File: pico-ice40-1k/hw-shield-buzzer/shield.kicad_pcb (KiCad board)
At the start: 2 copper layers, 58.4 x 41.3 mm, 31 parts, among them J1 JACK_TRS_6PINS, P1 CONN_01X12, P2 CONN_01X12, SW1 SPST, SW2 SW_PUSH, U1 TLV320DAC3203, U2 LD39015M18R, U3 SSM2305, U4 SSM2305

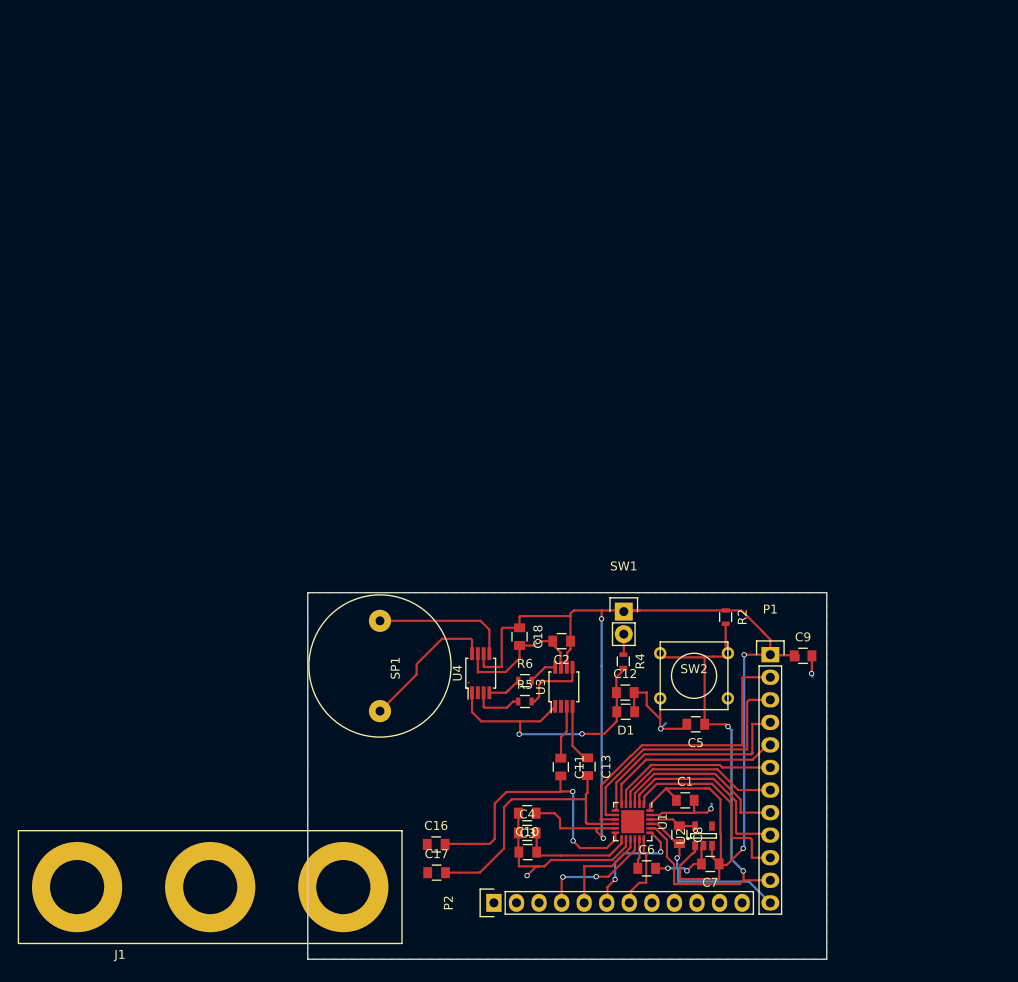
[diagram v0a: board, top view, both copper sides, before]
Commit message: new schema and PCB with lib for jack connector
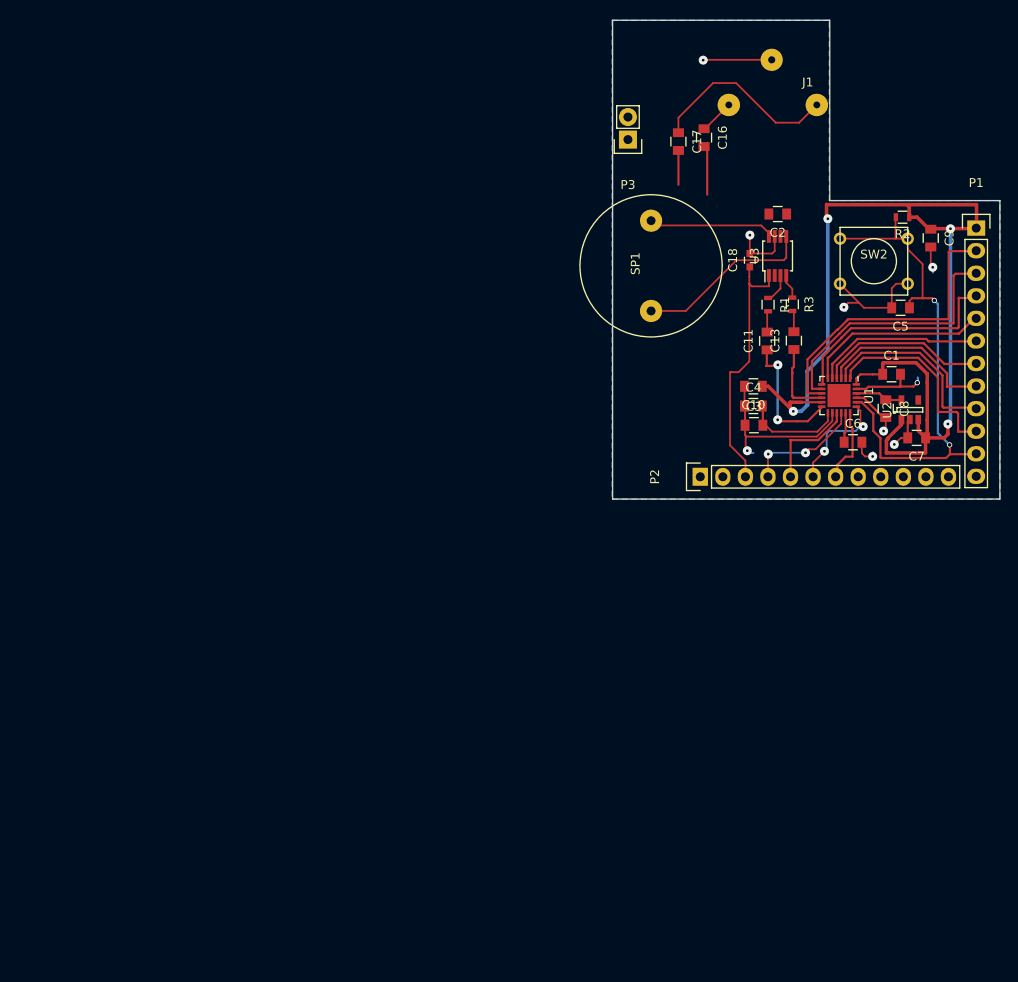
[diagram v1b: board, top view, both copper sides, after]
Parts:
- removed C12: 1u, Capacitors_SMD:C_0805
- removed D1: LED, Capacitors_SMD:C_0805
- removed R4: 1k, Resistors_SMD:R_0603
- removed R5, R6: 25k, Resistors_SMD:R_0603
- removed SW1: SPST, Pin_Headers:Pin_Header_Straight_1x02
- removed U4: SSM2305, Housings_SSOP:MSOP-8_3x3mm_Pitch0.65mm
- added P3: CONN_01X02, Pin_Headers:Pin_Header_Straight_1x02, F.Cu at (157.3, 63.9)
- added R1: 110k, Resistors_SMD:R_0603, F.Cu at (173.1, 82.5)
- added R3: 110k, Resistors_SMD:R_0603, F.Cu at (175.8, 82.5)
- C18: value 0.1u -> 1u; footprint Capacitors_SMD:C_0805 -> Capacitors_SMD:C_0603
- J1: footprint Connect:Banana_Jack_3Pin -> shield_foorprint:Jack Cliff FC68131
- U3: value SSM2305 -> TPA2005D1
- moved J1 113.0 mm to (167.4, 50.6), turned to 0 degrees
- moved C17 86.7 mm to (163.0, 64.2), turned to 270 degrees
- moved C16 85.1 mm to (165.9, 63.7), turned to 270 degrees
- moved SP1 54.4 mm to (159.9, 78.1), turned to 90 degrees
- moved C3 54.4 mm to (171.5, 96.1)
- moved C10 54.4 mm to (171.4, 91.7)
- moved C4 54.4 mm to (171.4, 93.9)
- moved U3 54.1 mm to (174.2, 77.0)
- moved C2 53.9 mm to (174.2, 72.3)
- moved P1 53.3 mm to (196.5, 73.9)
- moved U1 53.3 mm to (181.1, 92.7)
- moved C13 53.3 mm to (176.0, 86.6), turned to 90 degrees
- moved C6 53.3 mm to (182.7, 98.0)
- moved P2 53.3 mm to (165.5, 101.9)
- moved U2 53.3 mm to (189.1, 94.3)
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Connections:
- C11 pad 1: Net-(C11-Pad1) -> Haut-Parleur-L
- C11 pad 2: Haut-Parleur-L -> Net-(C11-Pad2)
- C13 pad 1: Net-(C13-Pad1) -> Haut-Parleur-R
- C13 pad 2: Haut-Parleur-R -> Net-(C13-Pad2)
- C18 pad 1: +3V3 -> /SD
- P2 pad 3: Net-(P2-Pad3) -> /SD
- U3 pad 1: Net-(C12-Pad1) -> /SD
- U3 pad 3: Net-(C11-Pad1) -> Net-(R1-Pad1)
- U3 pad 4: Net-(C13-Pad1) -> Net-(R3-Pad1)
- U3 pad 5: Net-(R5-Pad2) -> Net-(SP1-Pad1)
- U3 pad 6: +3V3 -> +5V
- U3 pad 8: Net-(R6-Pad2) -> Net-(SP1-Pad2)
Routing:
- net Net-(C12-Pad1): track 32.1 -> 0.00 mm, vias 2 -> 0
- net /SD: track 0.00 -> 29.4 mm
- net +3V3: track 154.1 -> 129.5 mm
- net Net-(C17-Pad1): track 0.00 -> 21.5 mm
- net Haut-Parleur-R: track 31.2 -> 13.1 mm
- net GND: track 92.1 -> 75.8 mm, vias 8 -> 9
- net Haut-Parleur-L: track 32.8 -> 20.3 mm
- net Net-(R5-Pad2): track 7.85 -> 0.00 mm
- net Net-(C13-Pad1): track 6.76 -> 0.00 mm
- net Net-(C11-Pad1): track 6.11 -> 0.00 mm
- net Net-(R5-Pad1): track 5.82 -> 0.00 mm
- net Net-(SP1-Pad1): track 15.4 -> 20.1 mm
- net Net-(R6-Pad1): track 4.01 -> 0.00 mm
- net Net-(C16-Pad1): track 0.00 -> 3.90 mm
- net Net-(R1-Pad1): track 0.00 -> 3.47 mm
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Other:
- board size 58.4 x 41.3 mm -> 43.6 x 53.9 mm
- net class Alim added: clearance 0.1524, trace_width 0.4, via_dia 1.016, via_drill 0.3048
- net class Default: clearance 0.2 -> 0.1524; trace_width 0.25 -> 0.2032; via_dia 0.6 -> 1.016; via_drill 0.4 -> 0.3048
- rule trace_clearance: 0.2 -> 0.1524

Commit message: Modif sch and pcb
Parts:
- removed C2: 0.1u, Capacitors_SMD:C_0805
- added C12: 0.1u, Capacitors_SMD:C_0805, F.Cu at (170.4, 73.7)
- C18: footprint Capacitors_SMD:C_0603 -> Capacitors_SMD:C_0805
- U3: footprint Housings_SSOP:MSOP-8_3x3mm_Pitch0.65mm -> Housings_SSOP:MSOP-8-1EP_3x3mm_Pitch0.65mm
- moved C17 14.7 mm to (177.4, 66.7)
- moved C16 5.76 mm to (170.8, 66.8)
- moved C18 3.53 mm to (174.1, 79.3), turned to 180 degrees
- moved U3 3.36 mm to (174.4, 73.7), turned to 180 degrees
- moved R1 2.32 mm to (175.4, 82.5)
- moved R3 1.40 mm to (177.2, 82.4)
- moved SP1 1.02 mm to (159.0, 78.5), turned to 270 degrees
- moved J1 0.43 mm to (167.5, 51.1)
- moved C8 0.42 mm to (186.3, 93.8)
- moved C11 0.16 mm to (172.9, 86.7)
- moved C13 0.14 mm to (175.9, 86.5)
- moved C6 0.14 mm to (182.5, 98.1)
- moved C10 0.05 mm to (171.5, 91.7)
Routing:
- net +5V: track 0.08 -> 34.3 mm
- net Haut-Parleur-L: track 20.3 -> 43.0 mm, vias 2 -> 3
- net Haut-Parleur-R: track 13.1 -> 32.0 mm
- net Net-(C17-Pad1): track 21.5 -> 7.58 mm
- net Net-(R3-Pad1): track 2.77 -> 10.9 mm
- net Net-(R1-Pad1): track 3.47 -> 10.3 mm
- net /RESET: track 58.3 -> 64.2 mm
- net +3V3: track 129.5 -> 124.9 mm
- net Net-(C16-Pad1): track 3.90 -> 8.42 mm
- net Net-(SP1-Pad2): track 14.2 -> 18.1 mm
- net Net-(SP1-Pad1): track 20.1 -> 16.3 mm
- net /SD: track 29.4 -> 32.6 mm
- net GND: track 75.8 -> 77.9 mm, vias 9 -> 7
- net Net-(C11-Pad2): track 2.53 -> 3.72 mm
- net MCBIAS: track 8.58 -> 9.10 mm
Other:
- net class Audio added: clearance 0.1524, trace_width 0.4, via_dia 1.016, via_drill 0.3048

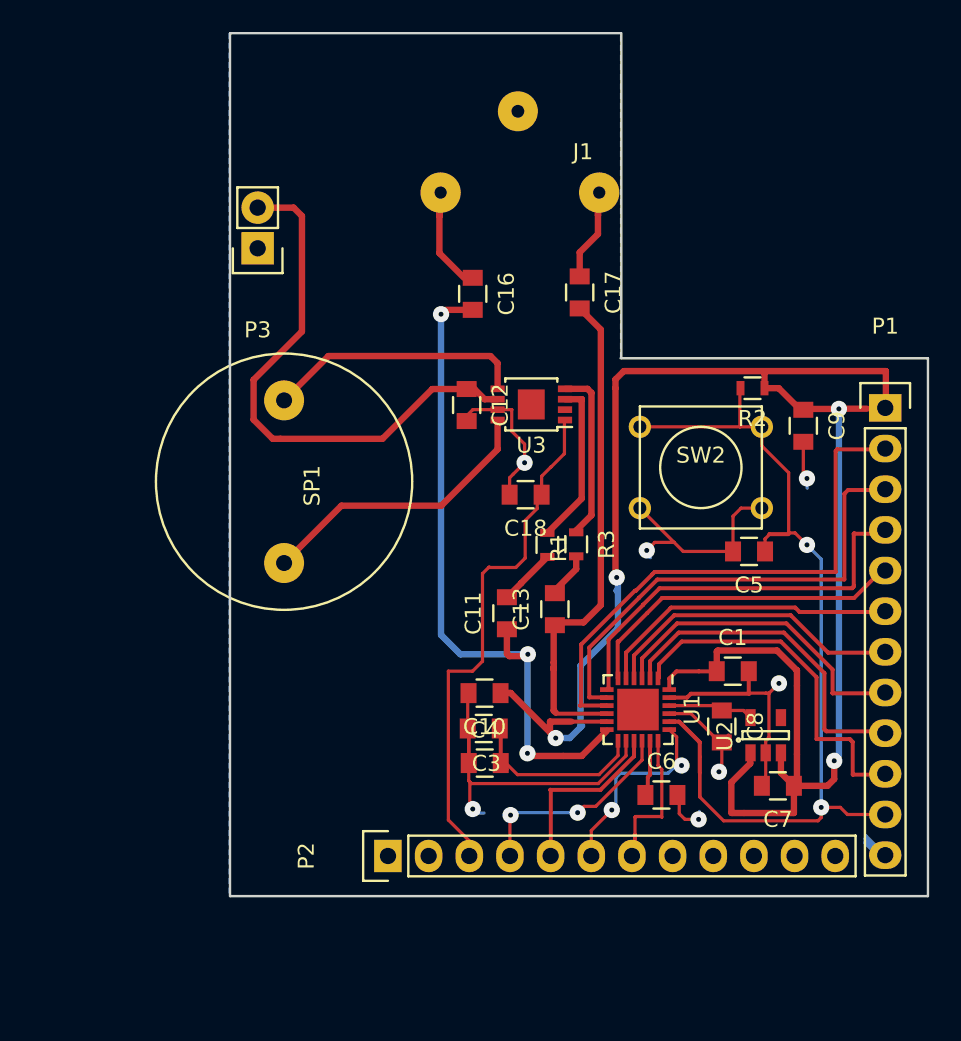
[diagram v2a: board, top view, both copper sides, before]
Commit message: update sch and pcb; add a speaker
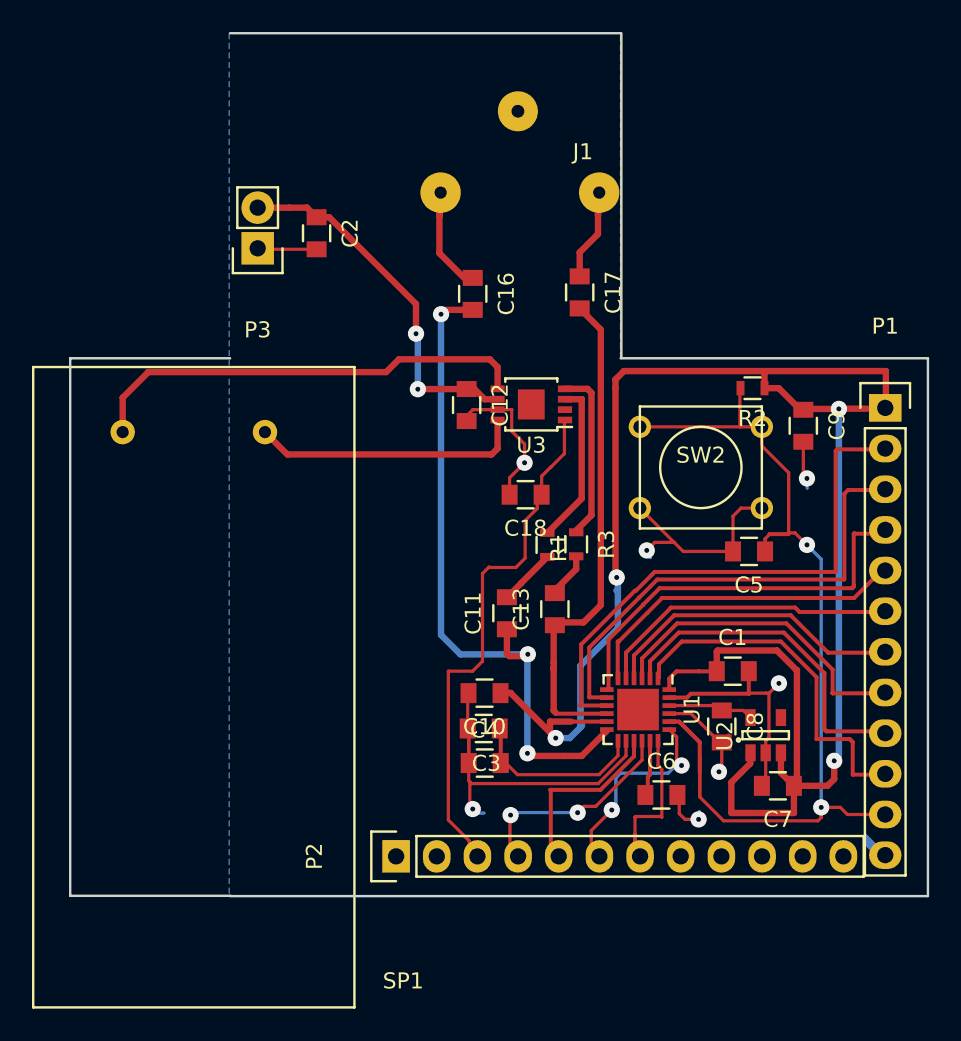
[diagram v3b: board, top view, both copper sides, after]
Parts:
- added C2: 10u, Capacitors_SMD:C_0805, F.Cu at (161.0, 63.0)
- SP1: footprint Buzzers_Beepers:BUZZER -> shield_foorprint:LOUDSPEAKER-ABS-216-RC
- moved SP1 33.1 mm to (163.4, 111.4), turned to 180 degrees
- moved P2 0.51 mm to (166.0, 101.9)
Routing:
- net Net-(SP1-Pad1): track 16.3 -> 28.1 mm
- net +5V: track 34.3 -> 23.0 mm, vias 0 -> 2
- net GND: track 77.9 -> 81.6 mm
- net Net-(SP1-Pad2): track 18.1 -> 17.0 mm
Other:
- board size 43.6 x 53.9 mm -> 53.6 x 53.9 mm

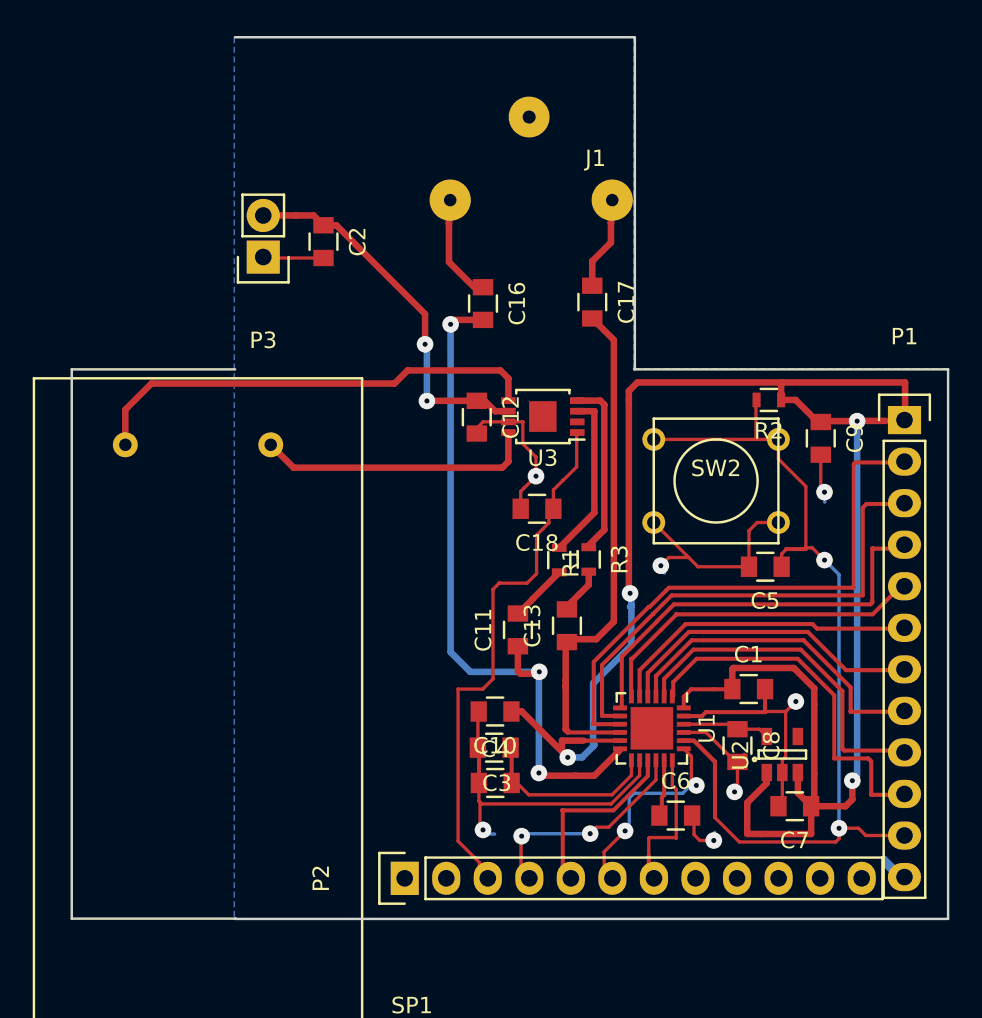
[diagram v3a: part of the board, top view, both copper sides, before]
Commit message: sch : Pull_up resistor added; Modif pcb; New files in .pretty
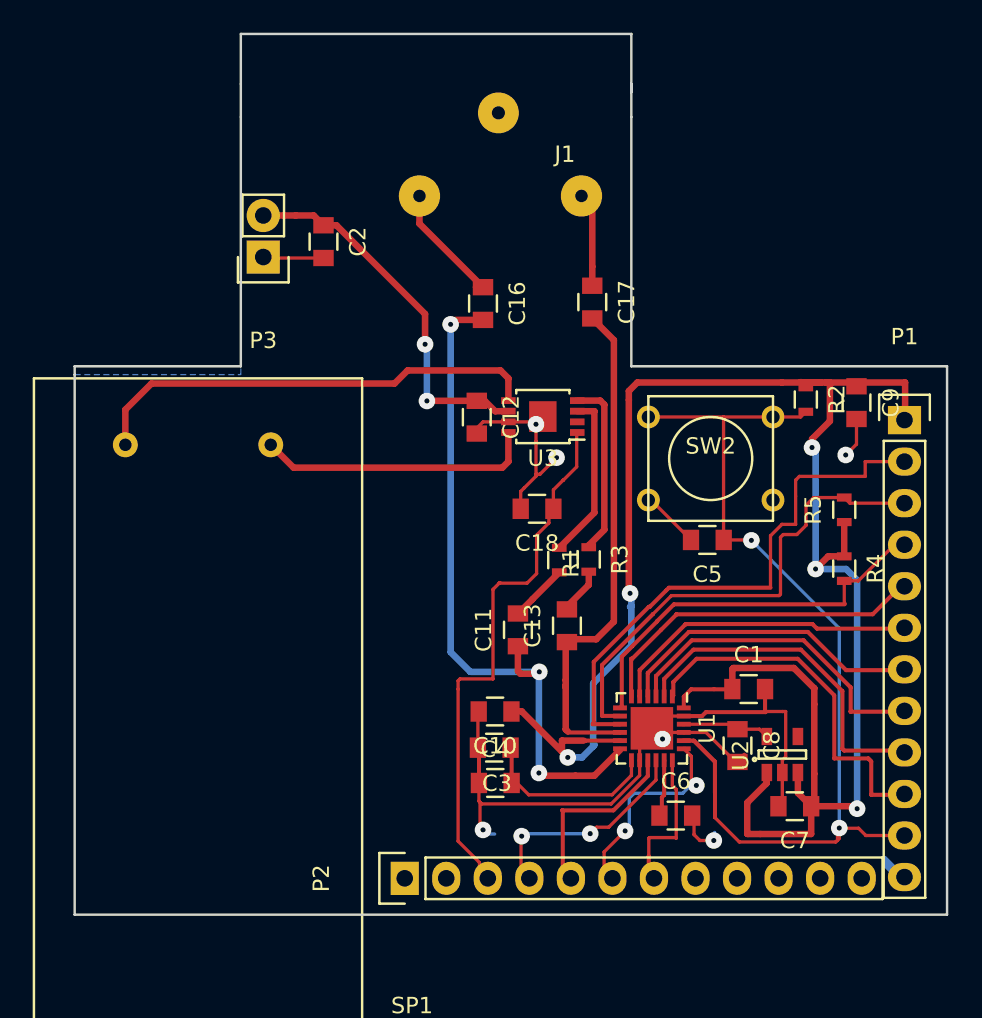
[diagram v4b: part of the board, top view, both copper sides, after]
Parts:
- added R4: 4.7k, Resistors_SMD:R_0603, F.Cu at (192.8, 83.0)
- added R5: 4.7k, Resistors_SMD:R_0603, F.Cu at (192.8, 79.4)
- P1, P2: value CONN_01X12 -> CONN_12
- moved C5 3.90 mm to (184.5, 81.2)
- moved C9 3.09 mm to (193.6, 72.8)
- moved R2 2.26 mm to (190.5, 72.6), turned to 270 degrees
- moved J1 1.90 mm to (165.6, 50.8)
- moved SW2 1.41 mm to (184.7, 76.3)
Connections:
- U1 pad 25: (no net) -> GND
- U3 pad 9: (no net) -> GND
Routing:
- net GND: track 81.6 -> 78.0 mm, vias 7 -> 6
- net Net-(C17-Pad1): track 7.58 -> 5.76 mm
- net +3V3: track 124.9 -> 126.6 mm, vias 4 -> 5
- net /RESET: track 64.2 -> 65.6 mm
- net SCL: track 25.4 -> 24.7 mm
- net Net-(C16-Pad1): track 8.42 -> 7.73 mm
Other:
- board size 53.6 x 53.9 mm -> 53.3 x 53.8 mm

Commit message: Small changes on the pcb
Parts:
- moved C10 0.42 mm to (171.7, 91.3)
- moved C9 0.10 mm to (193.5, 72.8)
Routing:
- net GND: track 78.0 -> 83.5 mm
